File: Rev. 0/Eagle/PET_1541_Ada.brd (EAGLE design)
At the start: 49 x 68 mm, 35 parts, among them IC1 74LS06N, IC2 74LS04N, J1 PET-USERPORT, J3 010599, J4 FCR681465P, SW6 JPT1236HB

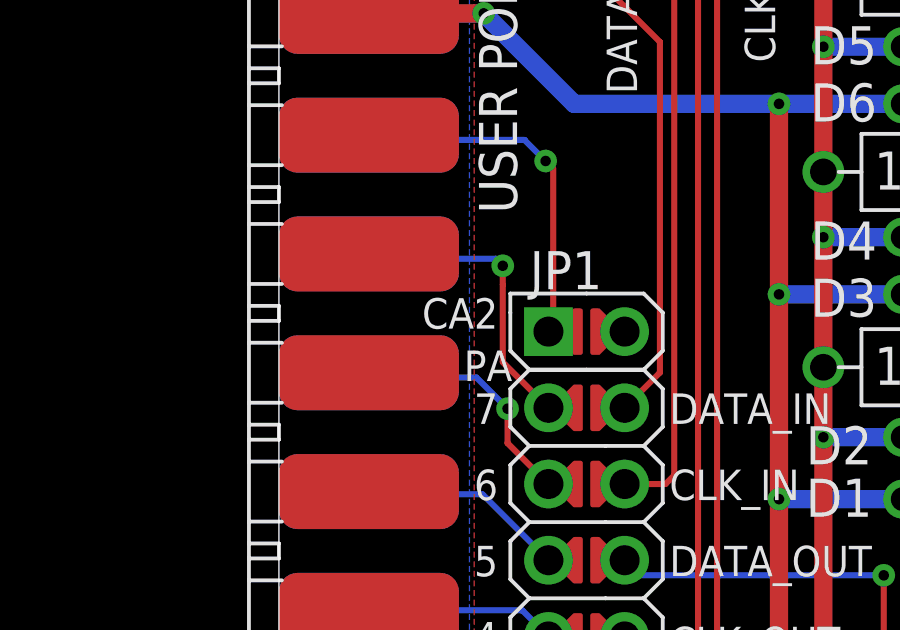
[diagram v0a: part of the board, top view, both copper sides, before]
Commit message: CB2 Silk screen fix
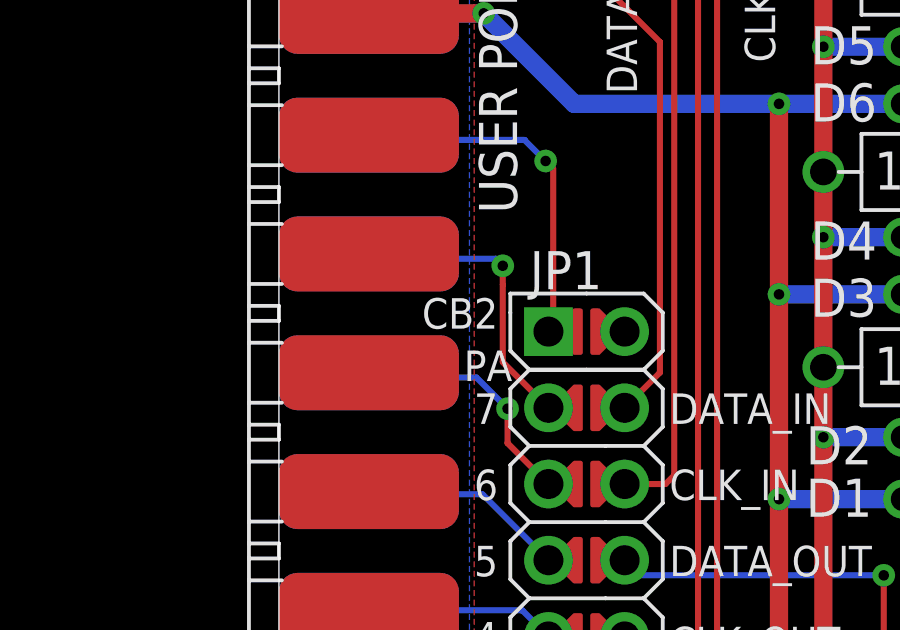
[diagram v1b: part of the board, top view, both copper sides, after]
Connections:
- net CA2 renamed CB2
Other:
- board text added: "CB2"
- board text removed: "CA2"
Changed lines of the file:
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@@
 <text x="7.3025" y="24.765" size="1.016" layer="21" align="center-right">0</text>
 <text x="7.46125" y="22.06625" size="1.016" layer="21" align="center-right">CA1</text>
-<text x="7.3025" y="45.87875" size="1.016" layer="21" align="center-right">CA2</text>
+<text x="7.3025" y="45.87875" size="1.016" layer="21" align="center-right">CB2</text>
 <text x="7.77875" y="44.1325" size="1.016" layer="21" align="center-right">PA</text>
 <text x="14.605" y="10.795" size="1.27" layer="25">1N5908</text>
@@
 <wire x1="6.985" y1="18.7325" x2="8.98375" y2="20.73125" width="0.2032" layer="1"/>
 </signal>
-<signal name="CA2">
+<signal name="CB2">
 <contactref element="J1" pad="M"/>
 <contactref element="JP1" pad="1"/>
